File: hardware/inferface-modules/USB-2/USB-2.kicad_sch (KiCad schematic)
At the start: 0 parts

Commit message: passive USB pass-through schematic
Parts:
- added J1: USB_device, symbol Connector:USB_A
- added J2: USB_PT, symbol Connector:USB_A
- added J3: Base_Board_Interface, symbol Connector_Generic:Conn_02x15_Odd_Even
- added R1, R2: 0ohm Removeable, symbol Device:R_Small_US
- added TP1, TP2, TP3, TP4: TestPoint, symbol Connector:TestPoint
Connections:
- new net: J1.2 (D-), R2.1
- new net: J1.3 (D+), R1.2, TP1.1
- new net: J2.2 (D-), R2.2, TP2.1
- new net: J2.3 (D+), R1.1
- new net GND: J1.4 (GND), J2.4 (GND), J3.13 (Pin_13), J3.23 (Pin_23), J3.29 (Pin_29), J3.7 (Pin_7), TP4.1
- new net MOD_PWR: J3.2 (Pin_2)
- new net V_USB: J1.1 (VBUS), J2.1 (VBUS), TP3.1
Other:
- note added: "Shield Strategy to be Decided Later"

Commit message: esd array implemented
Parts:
- added U1: TPD2E2U06QDBZRQ1, Package_TO_SOT_SMD:SOT-23, symbol Power_Protection:TPD2E2U06DCK
- R1: value 0ohm Removeable -> R_Small_US; footprint (none) -> Resistor_SMD:R_0805_2012Metric
- R2: value 0ohm Removeable -> 0R Jumpers; footprint (none) -> Resistor_SMD:R_0805_2012Metric
- TP1: value TestPoint -> D+; footprint (none) -> TestPoint:TestPoint_Pad_1.0x1.0mm
- TP2: value TestPoint -> D-; footprint (none) -> TestPoint:TestPoint_Pad_1.0x1.0mm
- TP3, TP4: footprint (none) -> TestPoint:TestPoint_Pad_1.0x1.0mm
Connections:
- net GND: now also U1.3
- net at J1.2 (D-), R2.1: now also U1.1
- net at R1.2, TP1.1: now also J2.3 (D+); no longer J1.3 (D+)
- net at R1.1: now also J1.3 (D+), U1.2; no longer J2.3 (D+)
- no-connect marks 0 -> 27
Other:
- moved on the sheet: J1, J2, J3, TP3

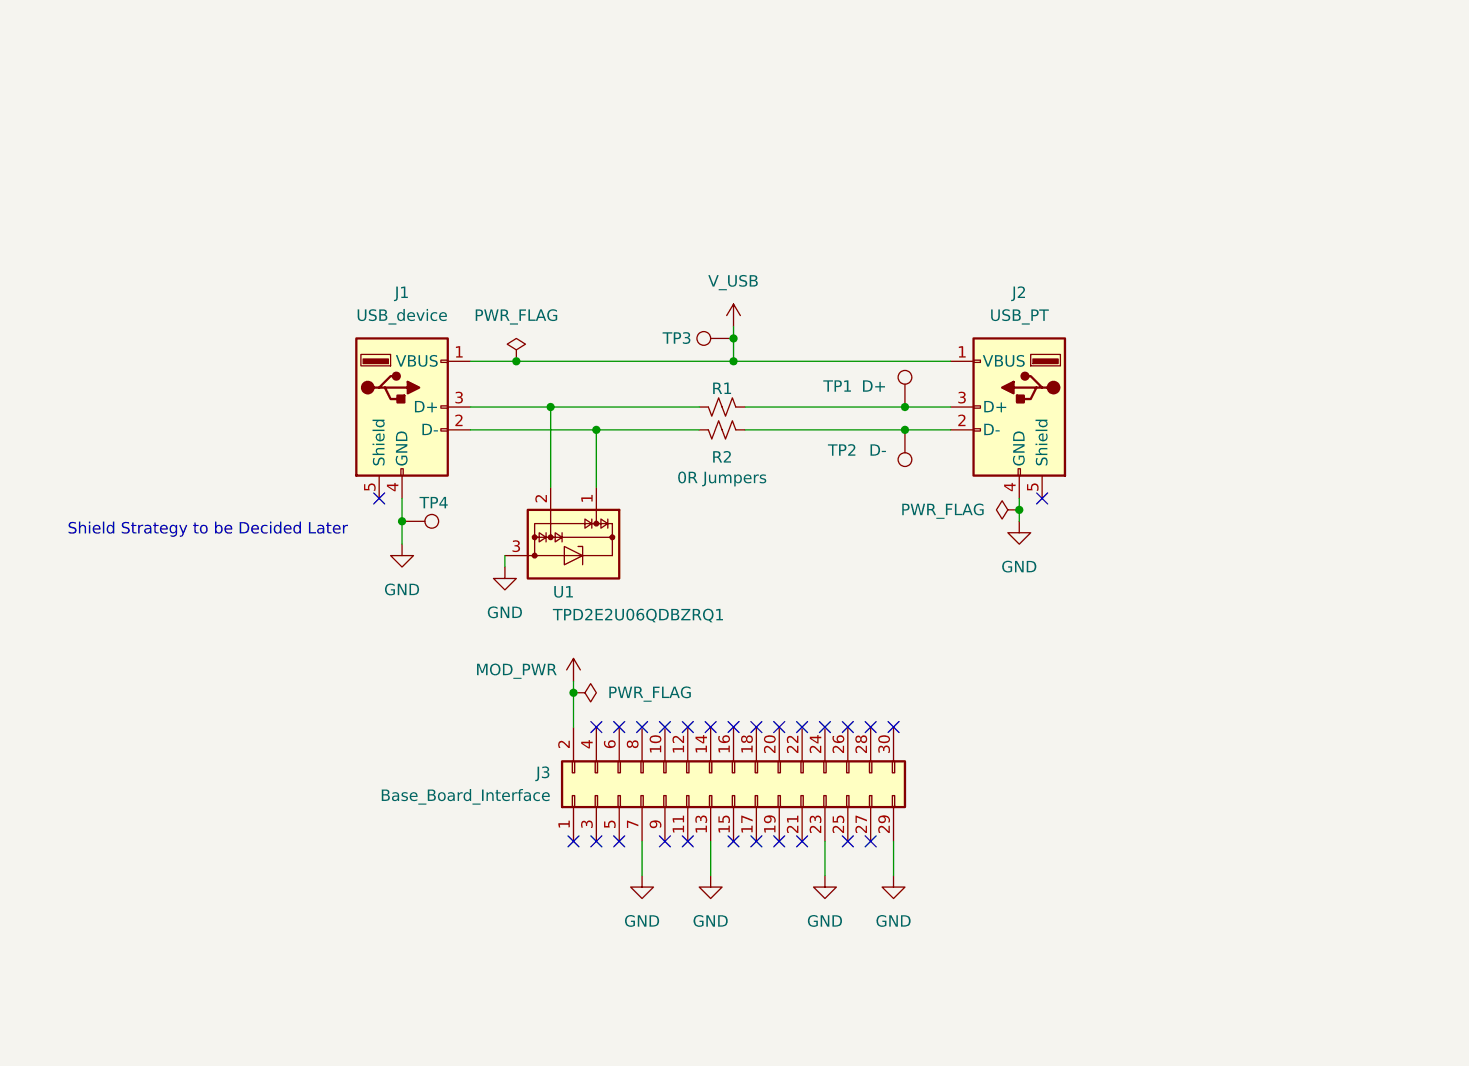
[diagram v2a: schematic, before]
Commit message: Add USB 2.0 PCB stack-up and critical placement
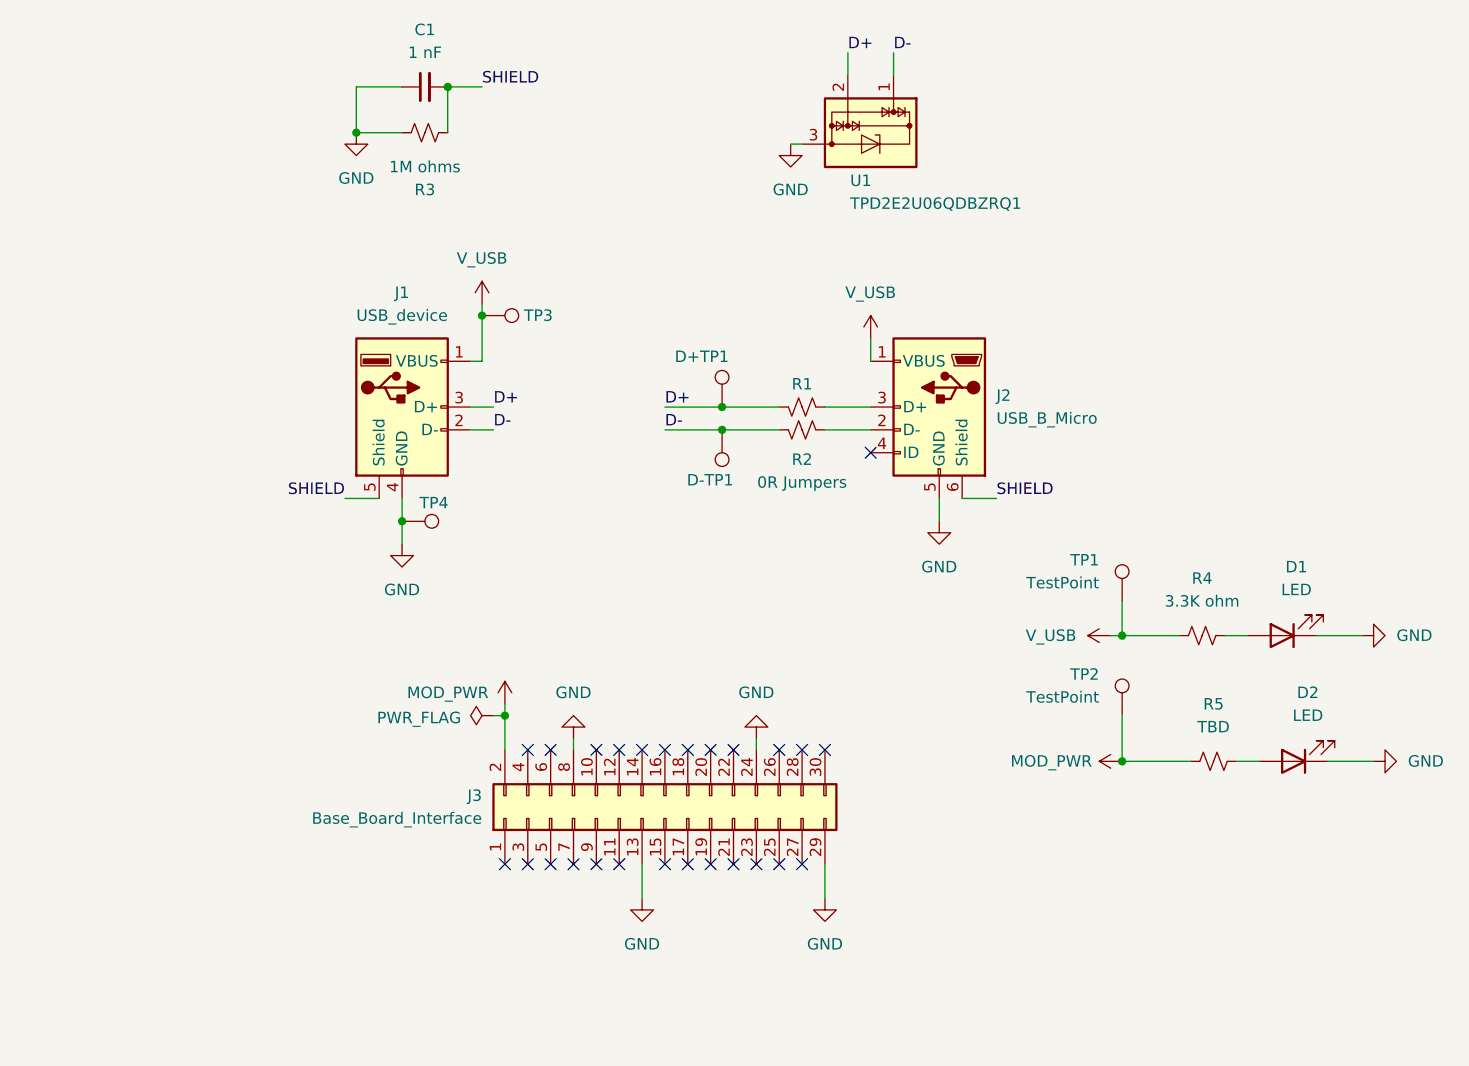
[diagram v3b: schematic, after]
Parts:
- removed J2: USB_PT, symbol Connector:USB_A
- added C1: 1 nF, Capacitor_SMD:C_1206_3216Metric, symbol Device:C_Small
- added D1, D2: LED, LED_SMD:LED_0805_2012Metric, symbol Device:LED
- added J2: USB_B_Micro, Connector_USB:USB_Micro-B_Molex_47346-0001, symbol Connector:USB_B_Micro
- added R3: 1M ohms, Resistor_SMD:R_0805_2012Metric, symbol Device:R_Small_US
- added R4: 3.3K ohm, Resistor_SMD:R_0805_2012Metric, symbol Device:R_Small_US
- added R5: TBD, Resistor_SMD:R_0805_2012Metric, symbol Device:R_Small_US
- added TP1, TP2: TestPoint, TestPoint:TestPoint_Pad_1.0x1.0mm, symbol Connector:TestPoint
- J1: footprint (none) -> Connector_USB:USB_A_Molex_67643_Horizontal
- J3: footprint (none) -> Connector_IDC:IDC-Header_2x15_P2.54mm_Vertical
- renumbered TP1 to D+TP1, TP2 to D-TP1
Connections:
- net GND: now also J3.24 (Pin_24), J3.8 (Pin_8), C1.1, D1.1 (K), D2.1 (K), J2.5 (GND), R3.1; no longer J3.23 (Pin_23), J3.7 (Pin_7)
- net MOD_PWR: now also R5.1, TP2.1
- net V_USB: now also J2.1 (VBUS), R4.1, TP1.1
- net D+: now reaches J1.3 (D+), R1.1, U1.2
- net D+: now also D+TP1.1
- net at R1.2: now also J2.3 (D+); no longer D+TP1.1
- net D-: now reaches J1.2 (D-), R2.1, U1.1
- net D-: now also D-TP1.1
- net SHIELD: now reaches J1.5 (Shield)
- net SHIELD: now also C1.2, J2.6 (Shield), R3.2
- net at R2.2: now also J2.2 (D-); no longer D-TP1.1
- new net: D1.2 (A), R4.2
- new net: D2.2 (A), R5.2
- no-connect marks 27 -> 26
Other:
- note removed: "Shield Strategy to be Decided Later"
- moved on the sheet: D+TP1, D-TP1, J3, R1, R2, TP3, U1
